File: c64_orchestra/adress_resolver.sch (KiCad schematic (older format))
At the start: 4 parts

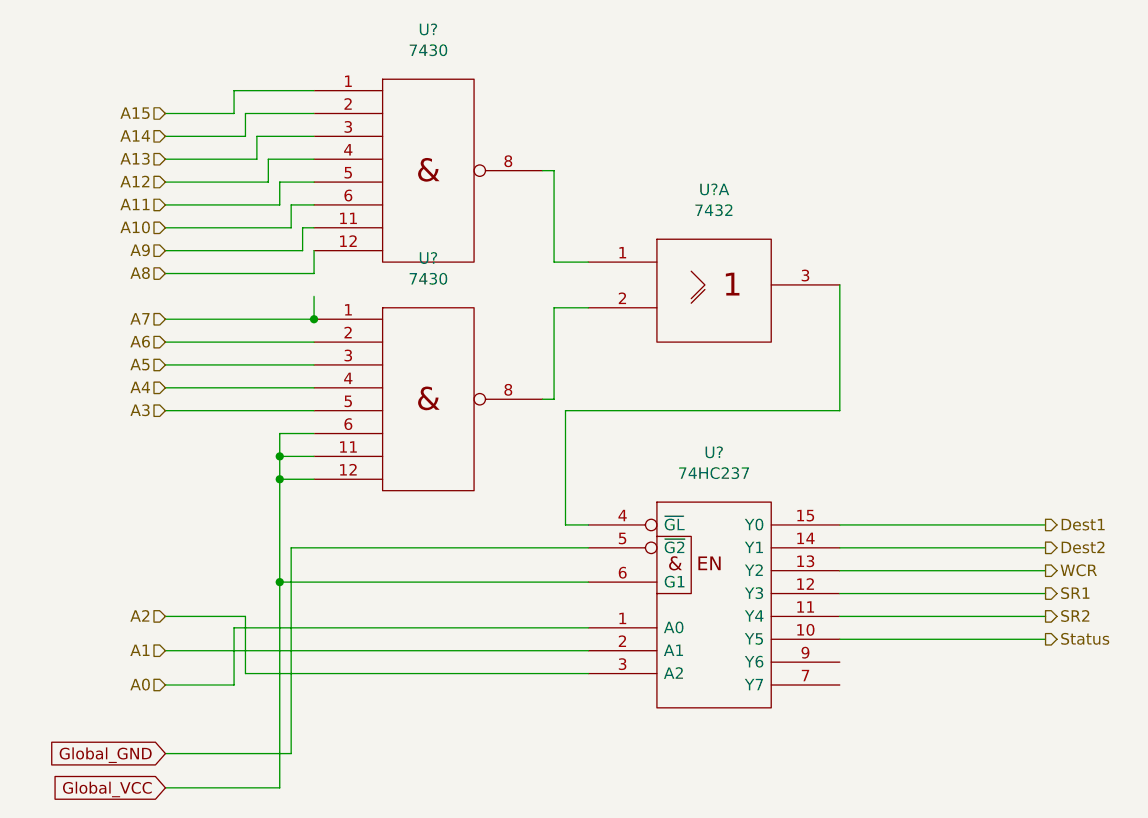
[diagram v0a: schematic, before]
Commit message: Added parts of schematic and worked on pcb layout.
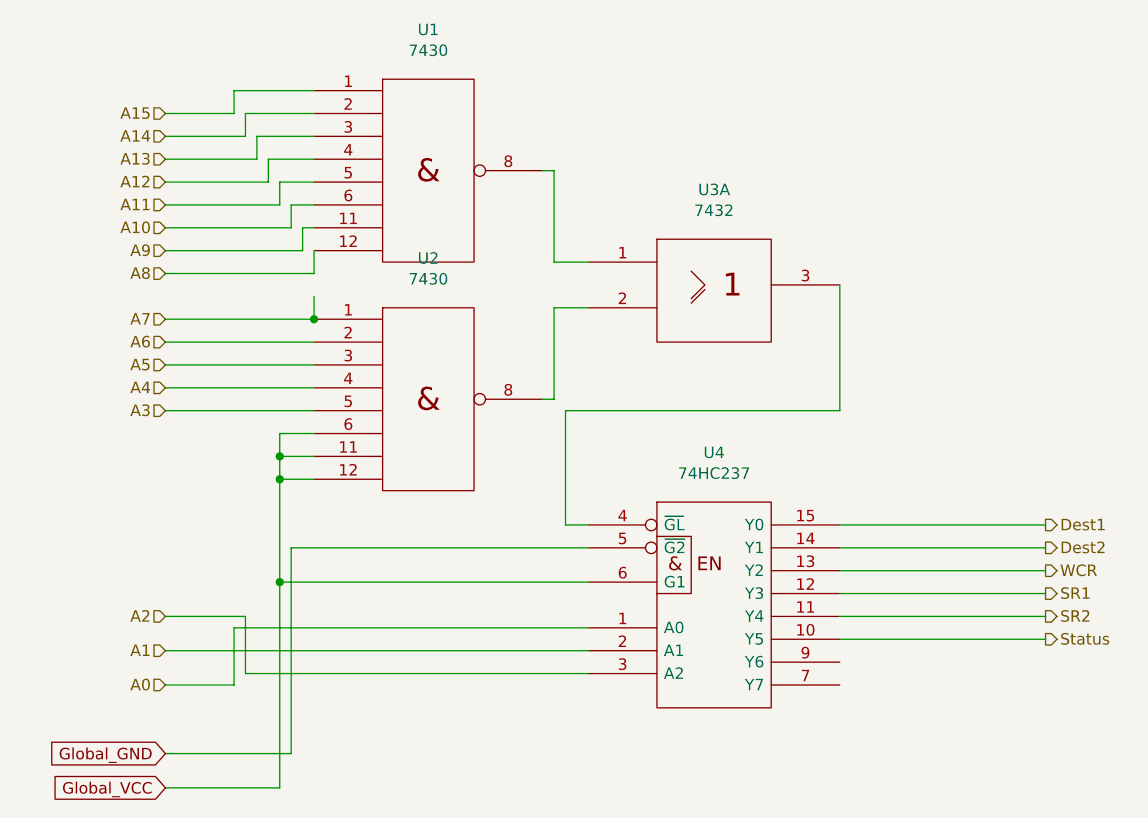
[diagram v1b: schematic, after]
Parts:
- U1, U2, U3: renamed from U?; footprint (none) -> Package_DIP:DIP-14_W7.62mm
- U4: renamed from U?; footprint (none) -> Package_DIP:DIP-16_W7.62mm
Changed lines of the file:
@@
 P 3400 4200
 AR Path="/5F9410D9" Ref="U?"  Part="1"
-AR Path="/5F92A19D/5F9410D9" Ref="U?"  Part="1"
-F 0 "U?" H 3400 4716 50  0000 C CNN
+AR Path="/5F92A19D/5F9410D9" Ref="U4"  Part="1"
+F 0 "U4" H 3400 4716 50  0000 C CNN
 F 1 "74HC237" H 3400 4625 50  0000 C CNN
-F 2 "" H 3400 4200 50  0001 C CNN
+F 2 "Package_DIP:DIP-16_W7.62mm" H 3400 4200 50  0001 C CNN
 F 3 "" H 3400 4200 50  0001 C CNN
 	1    3400 4200
@@
 P 2150 2450
 AR Path="/5F9410EA" Ref="U?"  Part="1"
-AR Path="/5F92A19D/5F9410EA" Ref="U?"  Part="1"
-F 0 "U?" H 2150 3066 50  0000 C CNN
+AR Path="/5F92A19D/5F9410EA" Ref="U1"  Part="1"
+F 0 "U1" H 2150 3066 50  0000 C CNN
 F 1 "7430" H 2150 2975 50  0000 C CNN
-F 2 "" H 2150 2450 50  0001 C CNN
+F 2 "Package_DIP:DIP-14_W7.62mm" H 2150 2450 50  0001 C CNN
 F 3 "" H 2150 2450 50  0001 C CNN
 	1    2150 2450
@@
 P 3400 2950
 AR Path="/5F9410F0" Ref="U?"  Part="1"
-AR Path="/5F92A19D/5F9410F0" Ref="U?"  Part="1"
-F 0 "U?" H 3400 3366 50  0000 C CNN
+AR Path="/5F92A19D/5F9410F0" Ref="U3"  Part="1"
+F 0 "U3" H 3400 3366 50  0000 C CNN
 F 1 "7432" H 3400 3275 50  0000 C CNN
-F 2 "" H 3400 2950 50  0001 C CNN
+F 2 "Package_DIP:DIP-14_W7.62mm" H 3400 2950 50  0001 C CNN
 F 3 "" H 3400 2950 50  0001 C CNN
 	1    3400 2950
@@
 P 2150 3450
 AR Path="/5F94109C" Ref="U?"  Part="1"
-AR Path="/5F92A19D/5F94109C" Ref="U?"  Part="1"
-F 0 "U?" H 2150 4066 50  0000 C CNN
+AR Path="/5F92A19D/5F94109C" Ref="U2"  Part="1"
+F 0 "U2" H 2150 4066 50  0000 C CNN
 F 1 "7430" H 2150 3975 50  0000 C CNN
-F 2 "" H 2150 3450 50  0001 C CNN
+F 2 "Package_DIP:DIP-14_W7.62mm" H 2150 3450 50  0001 C CNN
 F 3 "" H 2150 3450 50  0001 C CNN
 	1    2150 3450

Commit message: Changed the logic gates' numbering, changed some gates for todos.
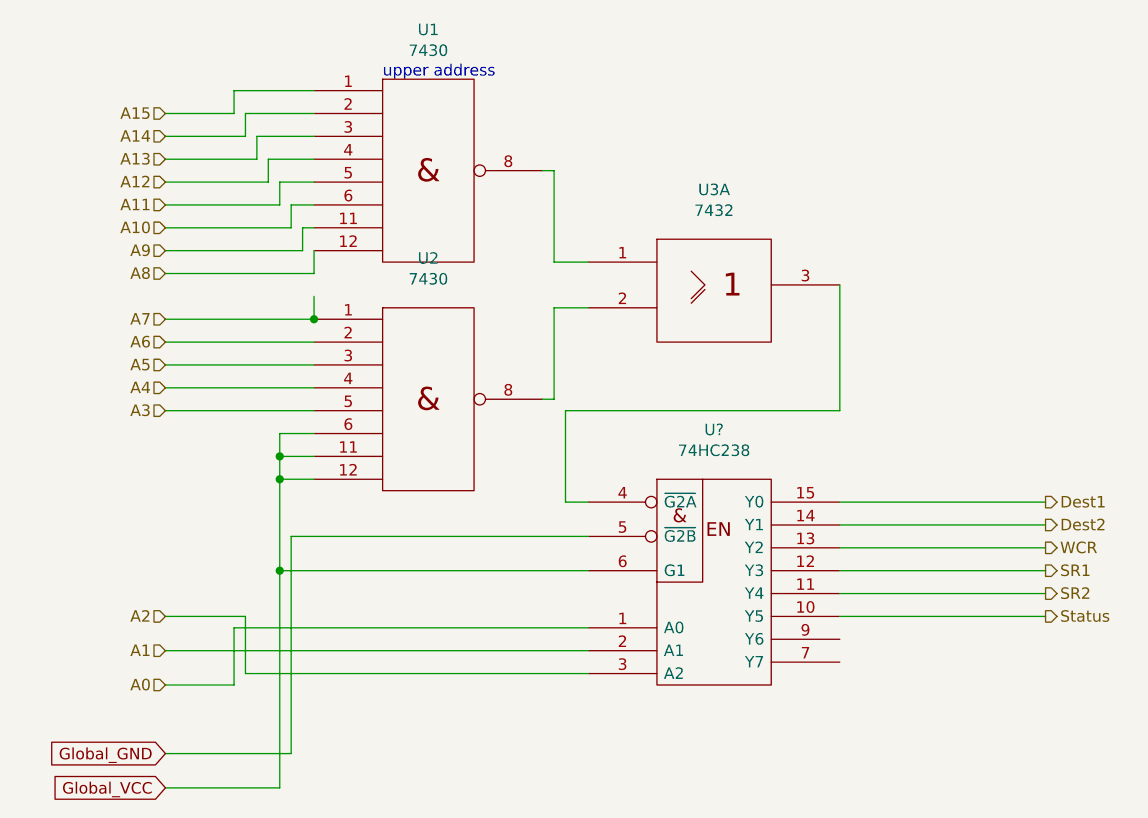
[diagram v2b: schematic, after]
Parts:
- removed U4: 74HC237, Package_DIP:DIP-16_W7.62mm, symbol 74xx_IEEE:74HC237
- added U?: 74HC238, symbol 74xx_IEEE:74HC238
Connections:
- net A0: now also U?.1 (A0)
- net A1: now also U?.2 (A1)
- net A2: now also U?.3 (A2)
- net Dest1: now also U?.15 (Y0)
- net Dest2: now also U?.14 (Y1)
- net GND: now also U?.8 (GND)
- net Global_GND: now also U?.5 (~G2B)
- net Global_VCC: now also U?.6 (G1)
- net SR1: now also U?.12 (Y3)
- net SR2: now also U?.11 (Y4)
- net Status: now also U?.10 (Y5)
- net VCC: now also U?.16 (VCC)
- net WCR: now also U?.13 (Y2)
- net at U3.3: now also U?.4 (~G2A)
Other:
- note added: "upper address"
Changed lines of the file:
@@
 Wire Wire Line
 	2700 3050 2850 3050
-$Comp
-L 74xx_IEEE:74HC237 U?
-U 1 1 5F9410D9
-P 3400 4200
-AR Path="/5F9410D9" Ref="U?"  Part="1"
-AR Path="/5F92A19D/5F9410D9" Ref="U4"  Part="1"
-F 0 "U4" H 3400 4716 50  0000 C CNN
-F 1 "74HC237" H 3400 4625 50  0000 C CNN
-F 2 "Package_DIP:DIP-16_W7.62mm" H 3400 4200 50  0001 C CNN
-F 3 "" H 3400 4200 50  0001 C CNN
-	1    3400 4200
-	1    0    0    -1
-$EndComp
 Wire Wire Line
 	1550 2600 1650 2600
@@
 Wire Wire Line
 	1300 2100 1650 2100
-$Comp
-L 74xx_IEEE:7430 U?
-U 1 1 5F9410EA
-P 2150 2450
-AR Path="/5F9410EA" Ref="U?"  Part="1"
-AR Path="/5F92A19D/5F9410EA" Ref="U1"  Part="1"
-F 0 "U1" H 2150 3066 50  0000 C CNN
-F 1 "7430" H 2150 2975 50  0000 C CNN
-F 2 "Package_DIP:DIP-14_W7.62mm" H 2150 2450 50  0001 C CNN
-F 3 "" H 2150 2450 50  0001 C CNN
-	1    2150 2450
-	1    0    0    -1
-$EndComp
 $Comp
 L 74xx_IEEE:7432 U?
@@
 Wire Wire Line
 	3950 3500 2750 3500
-Wire Wire Line
-	2750 3500 2750 4000
-Wire Wire Line
-	2750 4000 2850 4000
 Wire Wire Line
 	1000 2200 1300 2200
@@
 Wire Wire Line
 	1300 4450 2850 4450
+Text HLabel 4850 3900 2    50   Output ~ 0
+Dest1
 Text HLabel 4850 4000 2    50   Output ~ 0
-Dest1
-Text HLabel 4850 4100 2    50   Output ~ 0
 Dest2
 Wire Wire Line
@@
 Wire Wire Line
 	3950 4000 4850 4000
+Text HLabel 4850 4100 2    50   Output ~ 0
+WCR
 Text HLabel 4850 4200 2    50   Output ~ 0
-WCR
+SR1
 Text HLabel 4850 4300 2    50   Output ~ 0
-SR1
-Text HLabel 4850 4400 2    50   Output ~ 0
 SR2
 Wire Wire Line
@@
 Wire Wire Line
 	3950 4400 4850 4400
-Text HLabel 4850 4500 2    50   Output ~ 0
+Text HLabel 4850 4400 2    50   Output ~ 0
 Status
 Wire Wire Line
-	4850 4500 3950 4500
+	4850 3900 3950 3900
 Text GLabel 1000 5000 0    50   Input ~ 0
 Global_GND
@@
 Wire Wire Line
 	1000 5000 1550 5000
+$Comp
+L 74xx_IEEE:74HC238 U?
+U 1 1 5F8BC87D
+P 3400 4100
+F 0 "U?" H 3400 4616 50  0000 C CNN
+F 1 "74HC238" H 3400 4525 50  0000 C CNN
+F 2 "" H 3400 4100 50  0001 C CNN
+F 3 "" H 3400 4100 50  0001 C CNN
+	1    3400 4100
+	1    0    0    -1
+$EndComp
 Wire Wire Line
-	1550 4100 2850 4100
+	1500 3800 1500 4200
 Wire Wire Line
-	1550 4100 1550 5000
+	2850 4050 1550 4050
 Wire Wire Line
-	1500 4250 2850 4250
+	1550 4050 1550 5000
 Wire Wire Line
-	1500 3800 1500 4250
-Connection ~ 1500 4250
+	2850 4200 1500 4200
+Connection ~ 1500 4200
 Wire Wire Line
-	1500 4250 1500 5150
+	1500 4200 1500 5150
+Wire Wire Line
+	2850 3900 2750 3900
+Wire Wire Line
+	2750 3900 2750 3500
+Text Notes 1950 2050 0    50   ~ 0
+upper address
+$Comp
+L 74xx_IEEE:7430 U?
+U 1 1 5F9410EA
+P 2150 2450
+AR Path="/5F9410EA" Ref="U?"  Part="1"
+AR Path="/5F92A19D/5F9410EA" Ref="U1"  Part="1"
+F 0 "U1" H 2150 3066 50  0000 C CNN
+F 1 "7430" H 2150 2975 50  0000 C CNN
+F 2 "Package_DIP:DIP-14_W7.62mm" H 2150 2450 50  0001 C CNN
+F 3 "" H 2150 2450 50  0001 C CNN
+	1    2150 2450
+	1    0    0    -1
+$EndComp
 $EndSCHEMATC
